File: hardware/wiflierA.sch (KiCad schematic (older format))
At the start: 62 parts, among them CN1 10p, J1 AVRISP6, P1 WS2812, P10 SCL, P11 3V, P12 GND, P13 LED, P14 LED, P15 LED, P16 BAT, P17 TOUT, P18 AVRA0, P2 M0, P21 B+, P24 B-, P3 M1, P32 ESP_UART, P4 M2, P5 M3, P6 ANT, P9 SDA, Q1 7A_20V, Q2 7A_20V, Q3 7A_20V, Q4 7A_20V, U1 MCP1824/3.3, U2 MCP1824/3.3, U3 MPL3115A2, U4 LSM9DS1, U5 ESP8266EX, U6 W25Q80DV, U7 ATTINY441-QFN, X1 26MHz

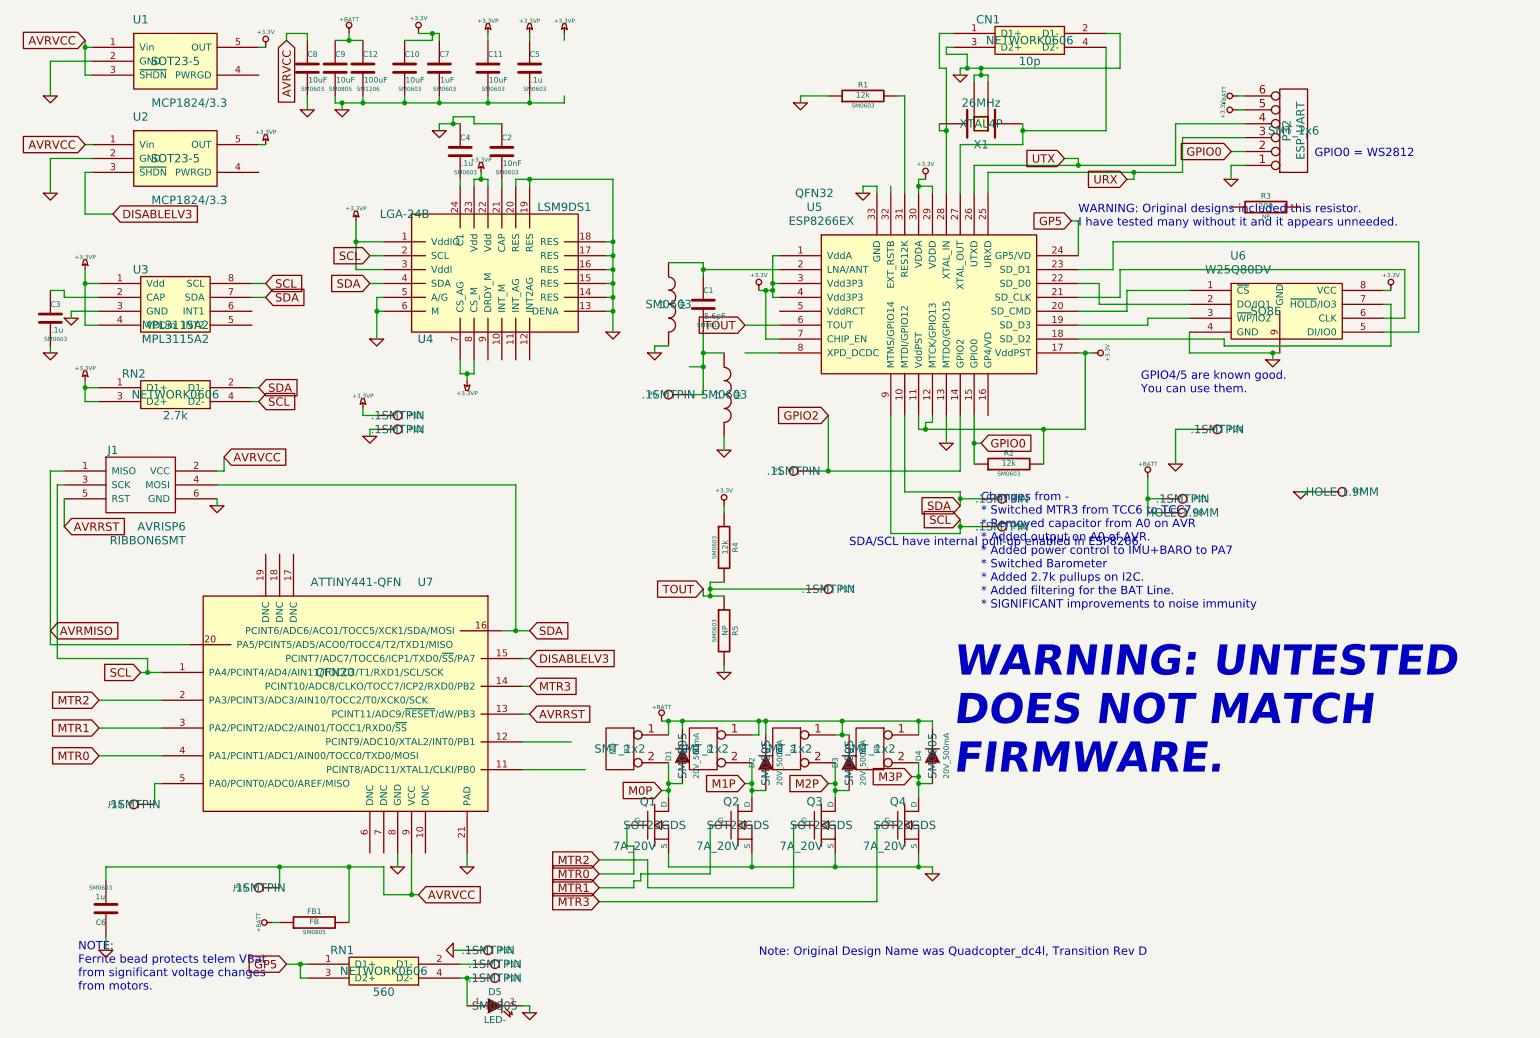
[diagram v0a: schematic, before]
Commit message: Update with driver for hand-held controllers
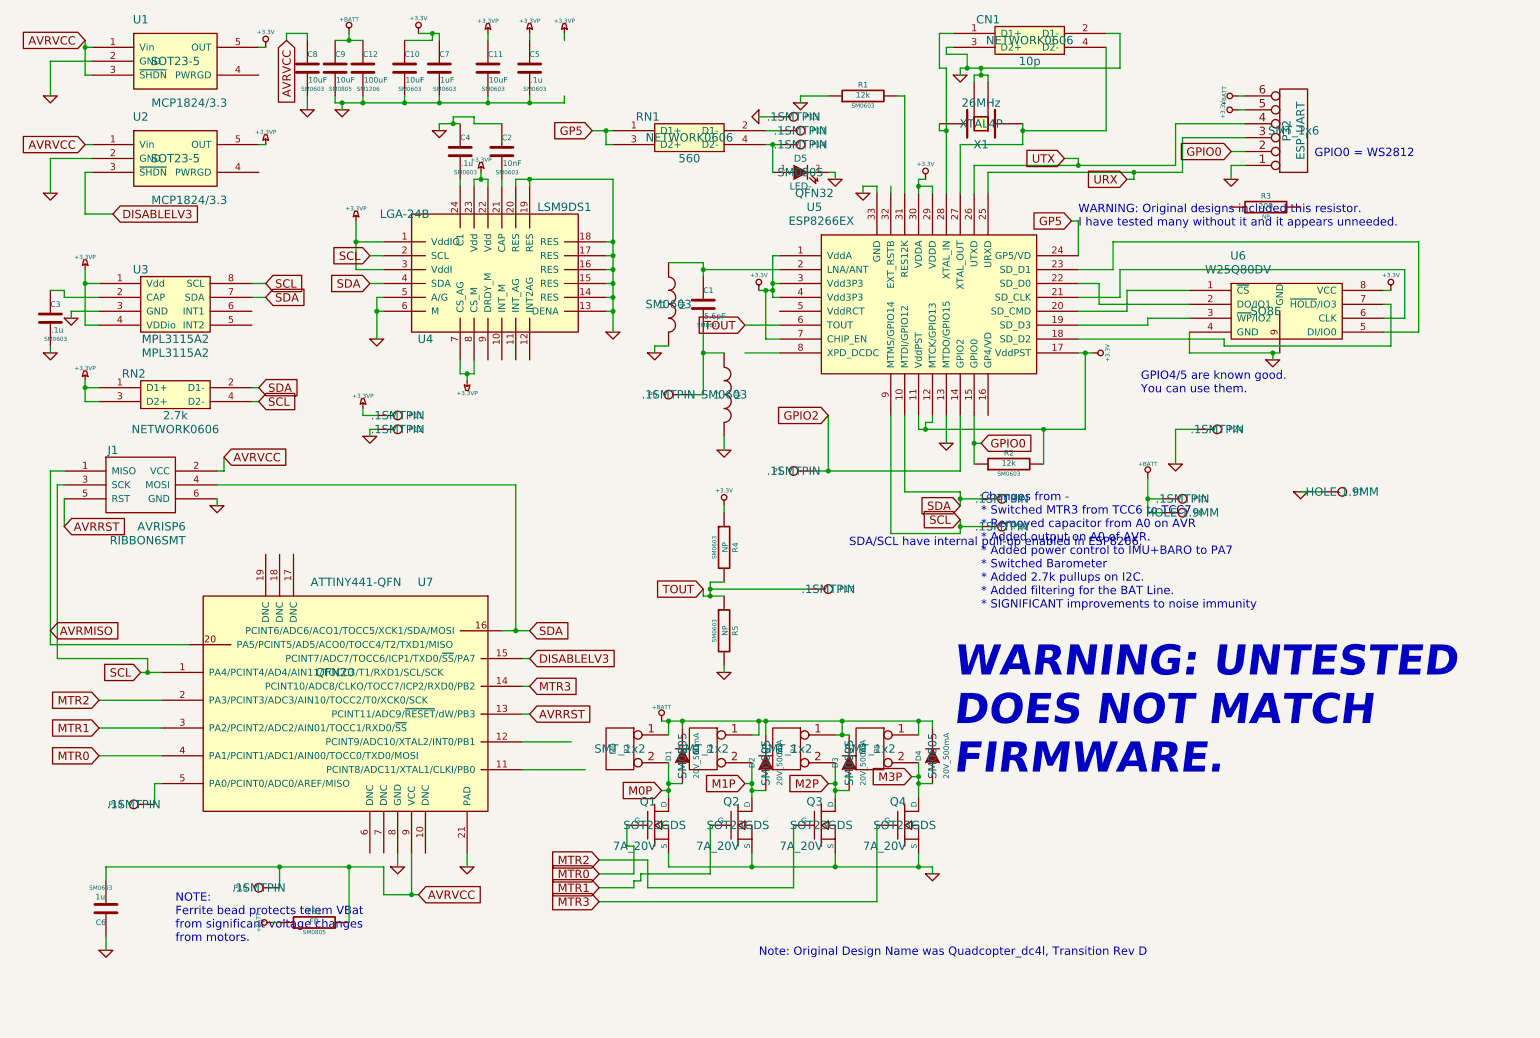
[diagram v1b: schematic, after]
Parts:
- P15: value LED -> GND
- P16: value BAT -> FLTBAT
- R4: value 12k -> NP; Cost .011 -> (none); Digikey 1276-4584-1-ND -> (none)
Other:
- moved on the sheet: D5, P13, P14, P15, RN1
